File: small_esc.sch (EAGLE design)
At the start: 46 parts, among them Q1 MOSFET-PCHANNELDPAKK, Q2 MOSFET-NCHANNELFDD8780, Q3 200mA/50V, Q4 MOSFET-PCHANNELDPAKK, Q5 MOSFET-NCHANNELFDD8780, Q6 200mA/50V, Q7 MOSFET-PCHANNELDPAKK, Q8 MOSFET-NCHANNELFDD8780, Q9 200mA/50V

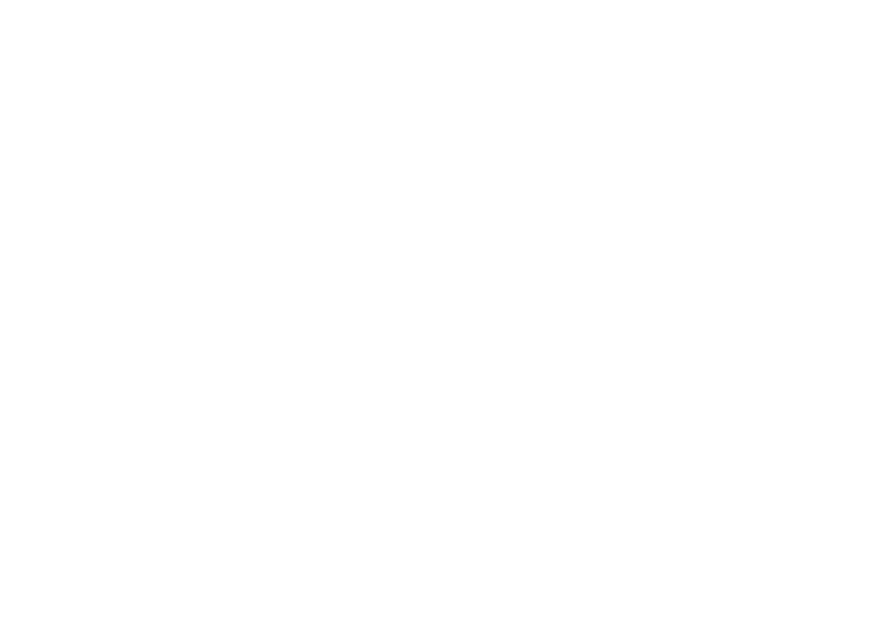
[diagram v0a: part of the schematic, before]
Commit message: add bypass capacitors
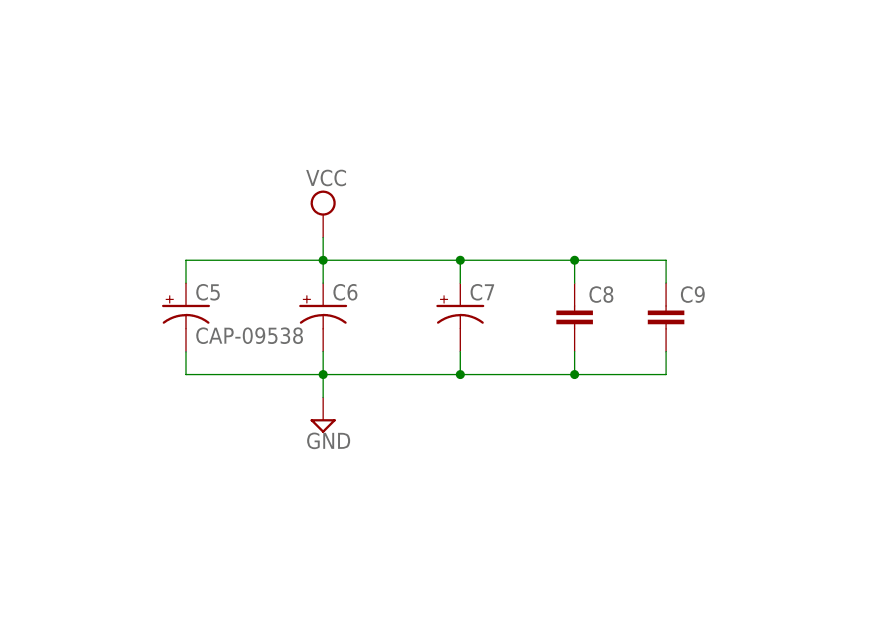
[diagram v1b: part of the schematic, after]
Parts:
- added C5: CAP-09538, SparkFun-Capacitors:1000UF-25V(PTH)
- added C6, C7: (no value), SparkFun-Capacitors:CAP_POLPTH2
- added C8, C9: (no value), SparkFun-Capacitors:0.1UF-50V-20%(PTH)KIT-EZ
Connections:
- net GND: now also C5.-, C6.-, C7.-, C8.2, C9.2
- net VCC: now also C5.+, C6.+, C7.+, C8.1, C9.1
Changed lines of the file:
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@@
 <setting verticaltext="up"/>
 </settings>
-<grid distance="0.1" unitdist="inch" unit="inch" style="lines" multiple="1" display="no" altdistance="0.01" altunitdist="inch" altunit="inch"/>
+<grid distance="0.1" unitdist="inch" unit="inch" style="lines" multiple="1" display="yes" altdistance="0.01" altunitdist="inch" altunit="inch"/>
 <layers>
 <layer number="1" name="Top" color="4" fill="1" visible="no" active="no"/>
@@
 <part name="JP5" library="SparkFun-Connectors" deviceset="M02" device="PTH3"/>
 <part name="JP6" library="SparkFun-Connectors" deviceset="M01" device="PTH_LONGPAD"/>
+<part name="C5" library="SparkFun-Capacitors" deviceset="1000UF-25V(PTH)" device="" value="CAP-09538"/>
+<part name="C6" library="SparkFun-Capacitors" deviceset="CAP_POL" device="PTH2"/>
+<part name="C7" library="SparkFun-Capacitors" deviceset="CAP_POL" device="PTH2"/>
+<part name="C8" library="SparkFun-Capacitors" deviceset="0.1UF-50V-20%(PTH)" device="KIT-EZ"/>
+<part name="C9" library="SparkFun-Capacitors" deviceset="0.1UF-50V-20%(PTH)" device="KIT-EZ"/>
+<part name="SUPPLY22" library="supply2" deviceset="VCC" device=""/>
+<part name="SUPPLY23" library="supply2" deviceset="GND" device=""/>
 </parts>
 <sheets>
@@
 <instance part="JP5" gate="G$1" x="-78.74" y="33.02"/>
 <instance part="JP6" gate="G$1" x="-78.74" y="17.78"/>
+<instance part="C5" gate="G$1" x="182.88" y="12.7"/>
+<instance part="C6" gate="G$1" x="198.12" y="12.7"/>
+<instance part="C7" gate="G$1" x="213.36" y="12.7"/>
+<instance part="C8" gate="G$1" x="226.06" y="10.16"/>
+<instance part="C9" gate="G$1" x="236.22" y="10.16"/>
+<instance part="SUPPLY22" gate="G$1" x="198.12" y="22.86"/>
+<instance part="SUPPLY23" gate="GND" x="198.12" y="0"/>
 </instances>
 <busses>
@@
 <label x="-66.04" y="35.56" size="1.778" layer="95"/>
 <junction x="-71.12" y="35.56"/>
+</segment>
+<segment>
+<pinref part="C5" gate="G$1" pin="+"/>
+<wire x1="182.88" y1="15.24" x2="182.88" y2="17.78" width="0.1524" layer="91"/>
+<wire x1="182.88" y1="17.78" x2="198.12" y2="17.78" width="0.1524" layer="91"/>
+<pinref part="C6" gate="G$1" pin="+"/>
+<wire x1="198.12" y1="17.78" x2="198.12" y2="15.24" width="0.1524" layer="91"/>
+<wire x1="198.12" y1="17.78" x2="213.36" y2="17.78" width="0.1524" layer="91"/>
+<junction x="198.12" y="17.78"/>
+<pinref part="C7" gate="G$1" pin="+"/>
+<wire x1="213.36" y1="17.78" x2="213.36" y2="15.24" width="0.1524" layer="91"/>
+<wire x1="213.36" y1="17.78" x2="226.06" y2="17.78" width="0.1524" layer="91"/>
+<junction x="213.36" y="17.78"/>
+<pinref part="C8" gate="G$1" pin="1"/>
+<wire x1="226.06" y1="17.78" x2="226.06" y2="15.24" width="0.1524" layer="91"/>
+<wire x1="226.06" y1="17.78" x2="236.22" y2="17.78" width="0.1524" layer="91"/>
+<junction x="226.06" y="17.78"/>
+<pinref part="C9" gate="G$1" pin="1"/>
+<wire x1="236.22" y1="17.78" x2="236.22" y2="15.24" width="0.1524" layer="91"/>
+<pinref part="SUPPLY22" gate="G$1" pin="VCC"/>
+<wire x1="198.12" y1="20.32" x2="198.12" y2="17.78" width="0.1524" layer="91"/>
 </segment>
 </net>
@@
 <label x="-66.04" y="17.78" size="1.778" layer="95"/>
 </segment>
+<segment>
+<pinref part="C5" gate="G$1" pin="-"/>
+<wire x1="182.88" y1="7.62" x2="182.88" y2="5.08" width="0.1524" layer="91"/>
+<wire x1="182.88" y1="5.08" x2="198.12" y2="5.08" width="0.1524" layer="91"/>
+<pinref part="C6" gate="G$1" pin="-"/>
+<wire x1="198.12" y1="5.08" x2="198.12" y2="7.62" width="0.1524" layer="91"/>
+<wire x1="198.12" y1="5.08" x2="213.36" y2="5.08" width="0.1524" layer="91"/>
+<junction x="198.12" y="5.08"/>
+<pinref part="C7" gate="G$1" pin="-"/>
+<wire x1="213.36" y1="5.08" x2="213.36" y2="7.62" width="0.1524" layer="91"/>
+<wire x1="213.36" y1="5.08" x2="226.06" y2="5.08" width="0.1524" layer="91"/>
+<junction x="213.36" y="5.08"/>
+<pinref part="C8" gate="G$1" pin="2"/>
+<wire x1="226.06" y1="5.08" x2="226.06" y2="7.62" width="0.1524" layer="91"/>
+<wire x1="226.06" y1="5.08" x2="236.22" y2="5.08" width="0.1524" layer="91"/>
+<junction x="226.06" y="5.08"/>
+<pinref part="C9" gate="G$1" pin="2"/>
+<wire x1="236.22" y1="5.08" x2="236.22" y2="7.62" width="0.1524" layer="91"/>
+<pinref part="SUPPLY23" gate="GND" pin="GND"/>
+<wire x1="198.12" y1="5.08" x2="198.12" y2="2.54" width="0.1524" layer="91"/>
+</segment>
 </net>
